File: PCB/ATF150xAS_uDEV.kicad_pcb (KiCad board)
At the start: 2 copper layers, 50.8 x 20.3 mm, 22 parts, among them J1 Conn_02x05_Odd_Even, J2 VERT, J3 VERT, U1 ATF150xASx-xAx44

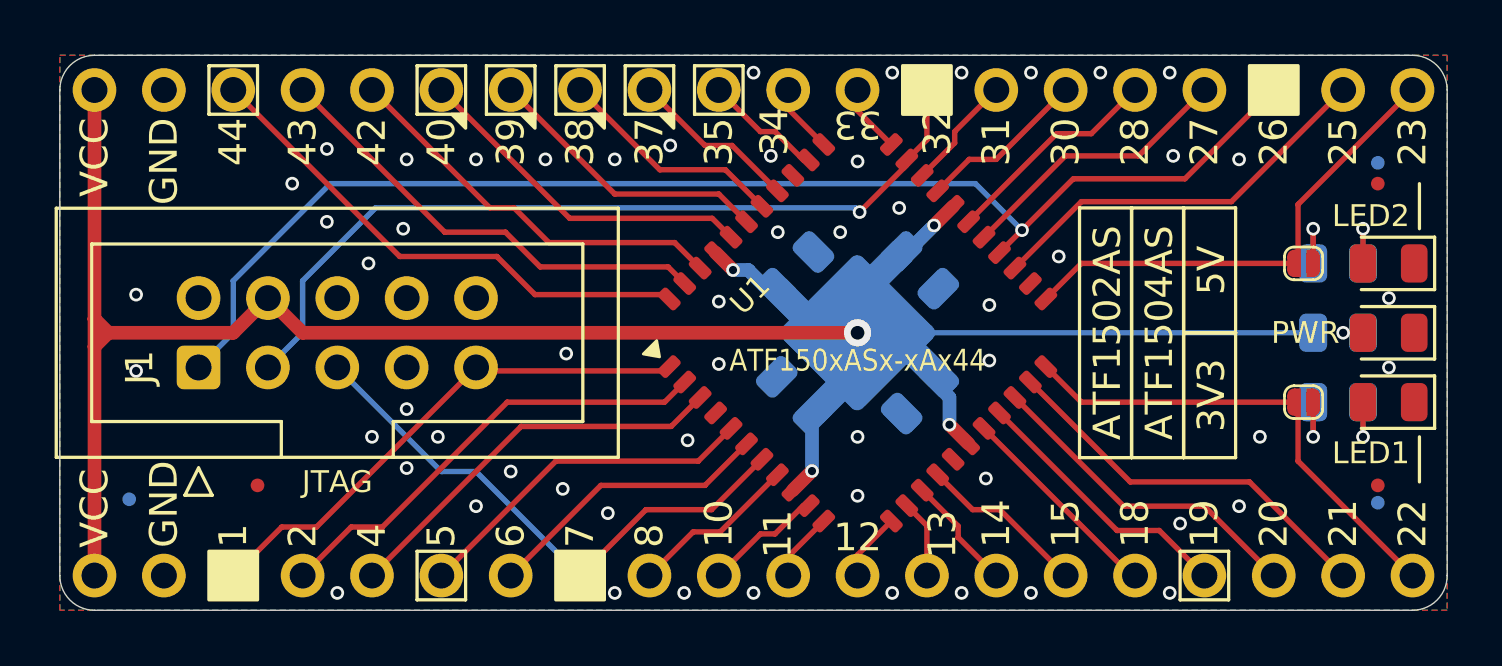
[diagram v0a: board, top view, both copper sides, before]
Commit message: tiny alignment of fiducials
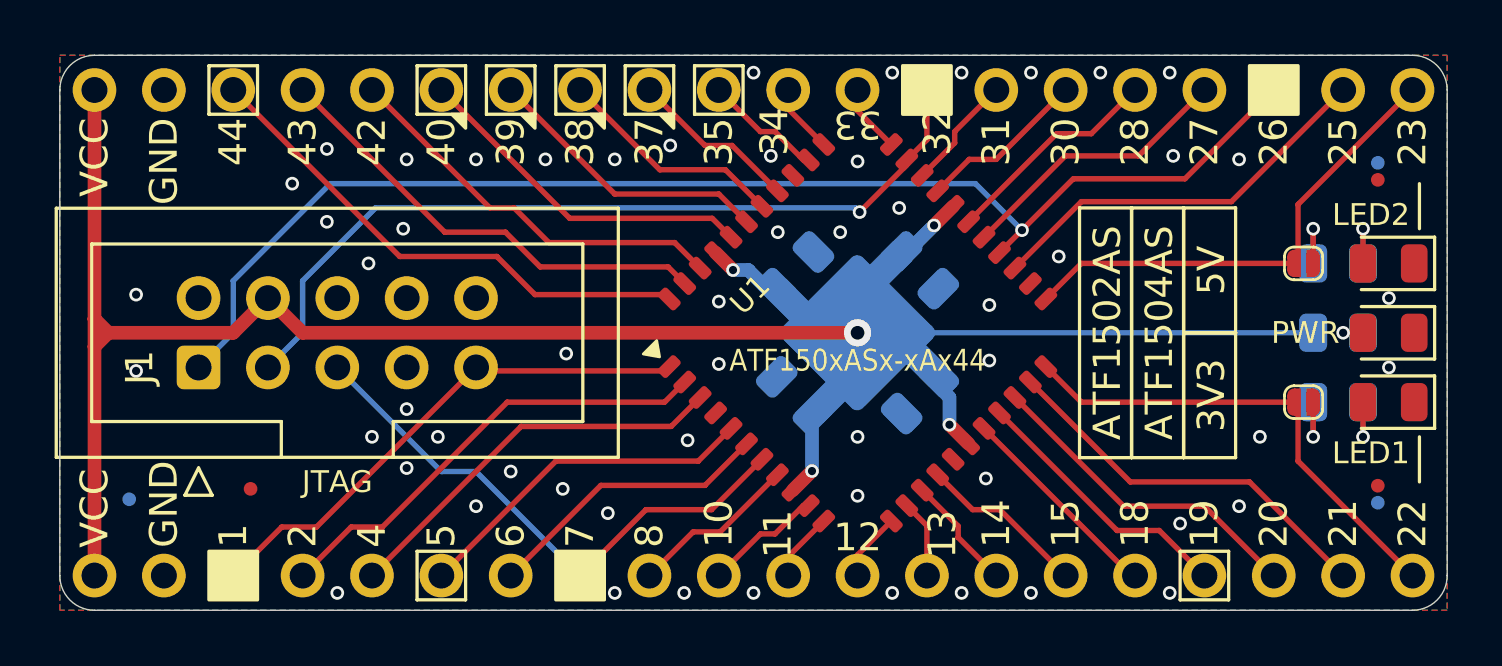
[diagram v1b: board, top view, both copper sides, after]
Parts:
- moved REF** 0.28 mm to (122.6, 106.0)
- moved REF** 0.14 mm to (163.8, 94.7)
